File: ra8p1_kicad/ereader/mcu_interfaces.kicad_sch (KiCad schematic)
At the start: 9 parts, among them U1 R7KA8P1KFLCAC#UC0

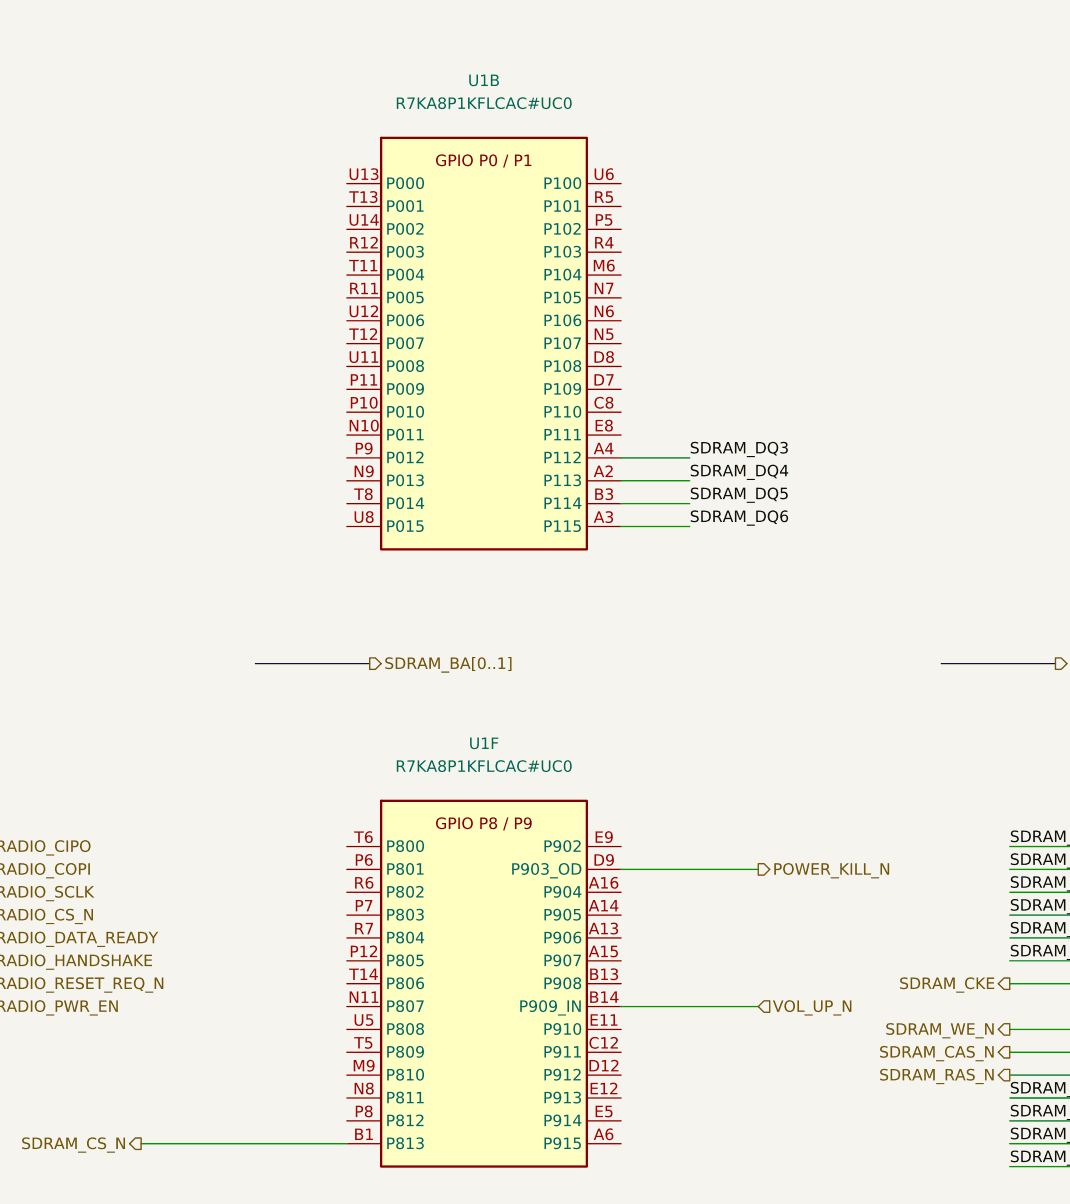
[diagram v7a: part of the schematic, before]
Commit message: Connect Octal NOR hierarchy and configured MCU pins
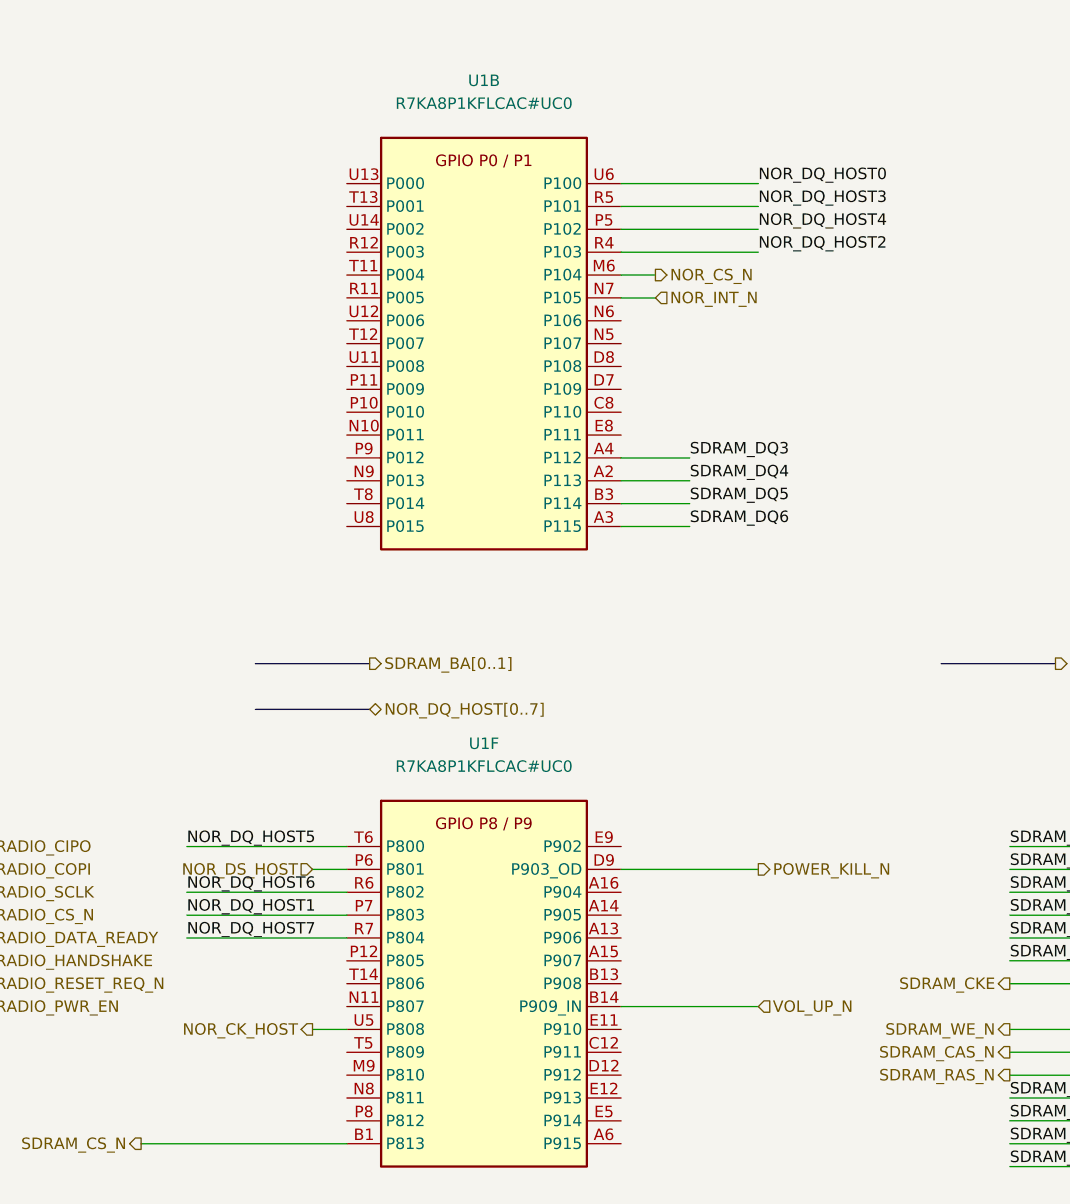
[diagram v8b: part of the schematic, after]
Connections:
- net NOR_DS_HOST: now reaches U1.P6 (P801)
- net NOR_DQ_HOST1: now reaches U1.P7 (P803)
- net NOR_DQ_HOST6: now reaches U1.R6 (P802)
- net NOR_DQ_HOST7: now reaches U1.R7 (P804)
- net NOR_DQ_HOST5: now reaches U1.T6 (P800)
- net NOR_CK_HOST: now reaches U1.U5 (P808)
- net NOR_CS_N: now reaches U1.M6 (P104)
- net NOR_INT_N: now reaches U1.N7 (P105)
- net NOR_DQ_HOST4: now reaches U1.P5 (P102)
- net NOR_DQ_HOST2: now reaches U1.R4 (P103)
- net NOR_DQ_HOST3: now reaches U1.R5 (P101)
- net NOR_DQ_HOST0: now reaches U1.U6 (P100)
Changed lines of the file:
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@@
+	(wire
+		(pts
+			(xy 167.64 58.42) (xy 171.45 58.42)
+		)
+		(stroke
+			(width 0)
+			(type default)
+		)
+	)
 	(wire
 		(pts
@@
 	(wire
 		(pts
+			(xy 167.64 55.88) (xy 182.88 55.88)
+		)
+		(stroke
+			(width 0)
+			(type default)
+		)
+	)
+	(wire
+		(pts
 			(xy 71.12 124.46) (xy 96.52 124.46)
 		)
@@
 		)
 	)
+	(bus
+		(pts
+			(xy 127 106.68) (xy 139.7 106.68)
+		)
+		(stroke
+			(width 0)
+			(type default)
+		)
+	)
 	(wire
 		(pts
@@
 	(wire
 		(pts
+			(xy 167.64 60.96) (xy 171.45 60.96)
+		)
+		(stroke
+			(width 0)
+			(type default)
+		)
+	)
+	(wire
+		(pts
 			(xy 71.12 137.16) (xy 96.52 137.16)
 		)
@@
 	(wire
 		(pts
+			(xy 167.64 53.34) (xy 182.88 53.34)
+		)
+		(stroke
+			(width 0)
+			(type default)
+		)
+	)
+	(wire
+		(pts
+			(xy 119.38 132.08) (xy 137.16 132.08)
+		)
+		(stroke
+			(width 0)
+			(type default)
+		)
+	)
+	(wire
+		(pts
 			(xy 17.78 144.78) (xy 40.64 144.78)
 		)
@@
 	(wire
 		(pts
+			(xy 133.35 124.46) (xy 137.16 124.46)
+		)
+		(stroke
+			(width 0)
+			(type default)
+		)
+	)
+	(wire
+		(pts
 			(xy 210.82 124.46) (xy 233.68 124.46)
 		)
@@
 	(wire
 		(pts
+			(xy 167.64 48.26) (xy 182.88 48.26)
+		)
+		(stroke
+			(width 0)
+			(type default)
+		)
+	)
+	(wire
+		(pts
 			(xy 304.8 205.74) (xy 304.8 213.36)
 		)
@@
 	(wire
 		(pts
+			(xy 133.35 142.24) (xy 137.16 142.24)
+		)
+		(stroke
+			(width 0)
+			(type default)
+		)
+	)
+	(wire
+		(pts
 			(xy 210.82 157.48) (xy 233.68 157.48)
 		)
@@
 	(wire
 		(pts
+			(xy 167.64 50.8) (xy 182.88 50.8)
+		)
+		(stroke
+			(width 0)
+			(type default)
+		)
+	)
+	(wire
+		(pts
+			(xy 119.38 129.54) (xy 137.16 129.54)
+		)
+		(stroke
+			(width 0)
+			(type default)
+		)
+	)
+	(wire
+		(pts
 			(xy 307.34 132.08) (xy 330.2 132.08)
 		)
@@
 		(pts
 			(xy 360.68 63.5) (xy 368.3 63.5)
+		)
+		(stroke
+			(width 0)
+			(type default)
+		)
+	)
+	(wire
+		(pts
+			(xy 119.38 127) (xy 137.16 127)
+		)
+		(stroke
+			(width 0)
+			(type default)
+		)
+	)
+	(wire
+		(pts
+			(xy 119.38 121.92) (xy 137.16 121.92)
 		)
 		(stroke
@@
 		)
 	)
+	(label "NOR_DQ_HOST6"
+		(at 119.38 127 0)
+		(effects
+			(font
+				(size 1.27 1.27)
+			)
+			(justify left bottom)
+		)
+	)
 	(label "SDRAM_DQ30"
 		(at 307.34 121.92 0)
@@
 		)
 	)
+	(label "NOR_DQ_HOST4"
+		(at 182.88 53.34 0)
+		(effects
+			(font
+				(size 1.27 1.27)
+			)
+			(justify left bottom)
+		)
+	)
 	(label "SDRAM_DQ31"
 		(at 17.78 139.7 0)
@@
 		)
 	)
+	(label "NOR_DQ_HOST7"
+		(at 119.38 132.08 0)
+		(effects
+			(font
+				(size 1.27 1.27)
+			)
+			(justify left bottom)
+		)
+	)
+	(label "NOR_DQ_HOST2"
+		(at 182.88 55.88 0)
+		(effects
+			(font
+				(size 1.27 1.27)
+			)
+			(justify left bottom)
+		)
+	)
 	(label "SDRAM_DQ7"
 		(at 17.78 144.78 0)
@@
 		)
 	)
+	(label "NOR_DQ_HOST0"
+		(at 182.88 48.26 0)
+		(effects
+			(font
+				(size 1.27 1.27)
+			)
+			(justify left bottom)
+		)
+	)
 	(label "SDRAM_BA1"
 		(at 307.34 160.02 0)
@@
 		)
 	)
+	(label "NOR_DQ_HOST1"
+		(at 119.38 129.54 0)
+		(effects
+			(font
+				(size 1.27 1.27)
+			)
+			(justify left bottom)
+		)
+	)
 	(label "SDRAM_DQ15"
 		(at 17.78 154.94 0)
@@
 		)
 	)
+	(label "NOR_DQ_HOST5"
+		(at 119.38 121.92 0)
+		(effects
+			(font
+				(size 1.27 1.27)
+			)
+			(justify left bottom)
+		)
+	)
 	(label "SDRAM_DQ17"
 		(at 307.34 154.94 0)
@@
 	(label "SDRAM_DQ16"
 		(at 307.34 157.48 0)
+		(effects
+			(font
+				(size 1.27 1.27)
+			)
+			(justify left bottom)
+		)
+	)
+	(label "NOR_DQ_HOST3"
+		(at 182.88 50.8 0)
 		(effects
 			(font
@@
 		)
 	)
+	(hierarchical_label "NOR_INT_N"
+		(shape input)
+		(at 171.45 60.96 0)
+		(effects
+			(font
+				(size 1.27 1.27)
+			)
+			(justify left)
+		)
+	)
 	(hierarchical_label "VOL_UP_N"
 		(shape input)
@@
 		)
 	)
+	(hierarchical_label "NOR_CK_HOST"
+		(shape output)
+		(at 133.35 142.24 180)
+		(effects
+			(font
+				(size 1.27 1.27)
+			)
+			(justify right)
+		)
+	)
 	(hierarchical_label "VOL_DOWN_N"
 		(shape input)
@@
 		)
 	)
+	(hierarchical_label "NOR_DS_HOST"
+		(shape input)
+		(at 133.35 124.46 180)
+		(effects
+			(font
+				(size 1.27 1.27)
+			)
+			(justify right)
+		)
+	)
 	(hierarchical_label "RADIO_SCLK"
 		(shape output)
@@
 		)
 	)
+	(hierarchical_label "NOR_CS_N"
+		(shape output)
+		(at 171.45 58.42 0)
+		(effects
+			(font
+				(size 1.27 1.27)
+			)
+			(justify left)
+		)
+	)
 	(hierarchical_label "RADIO_CS_N"
 		(shape output)
@@
 		(effects
 			(font
+				(size 1.27 1.27)
+			)
+			(justify left)
+		)
+	)
+	(hierarchical_label "NOR_DQ_HOST[0..7]"
+		(shape bidirectional)
+		(at 139.7 106.68 0)
+		(effects
+			(font
